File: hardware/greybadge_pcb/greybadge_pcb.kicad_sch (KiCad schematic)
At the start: 73 parts, among them J1 Conn_02x05_Row_Letter_First, J2 Conn_02x05_Row_Letter_First, J3 Conn_02x05_Row_Letter_First, J4 Conn_02x05_Row_Letter_First, SW1 SW_Push, SW2 SW_Push, SW3 SW_Push, SW4 SW_Push, SW5 SW_Push, SW6 SW_Push, SW7 SW_Push, U1 TLV62568DBV, U2 TLV62568DBV, U3 TLV73325PDBV

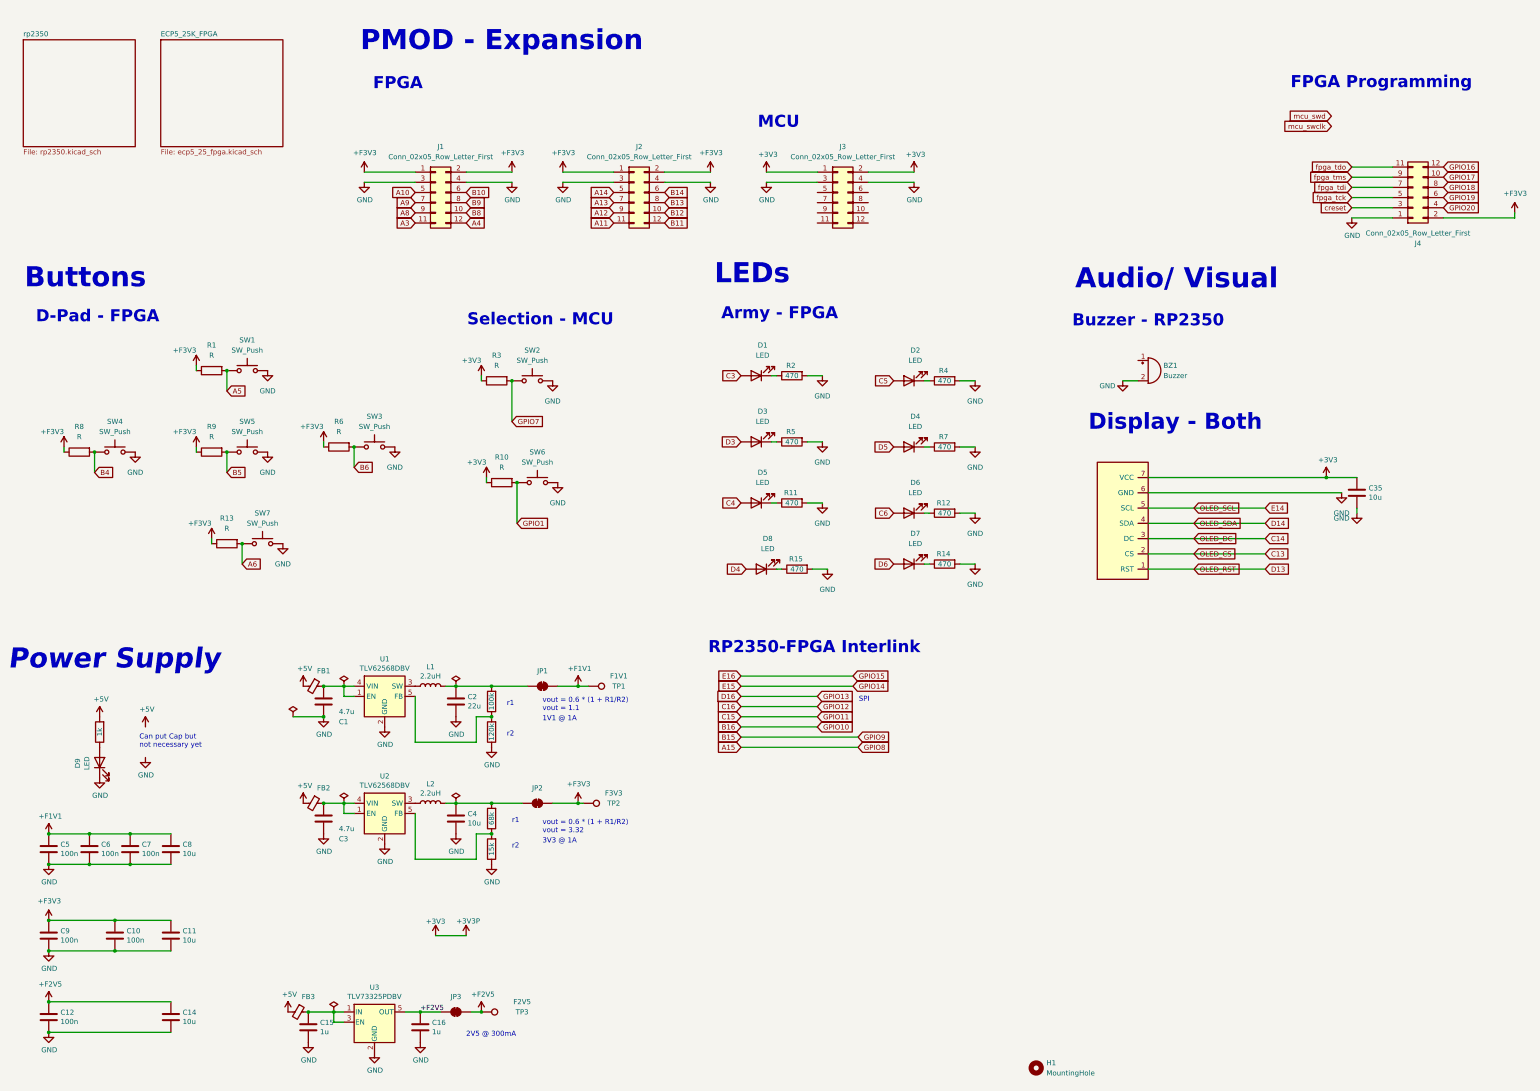
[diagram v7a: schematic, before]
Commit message: feat: add lipo support
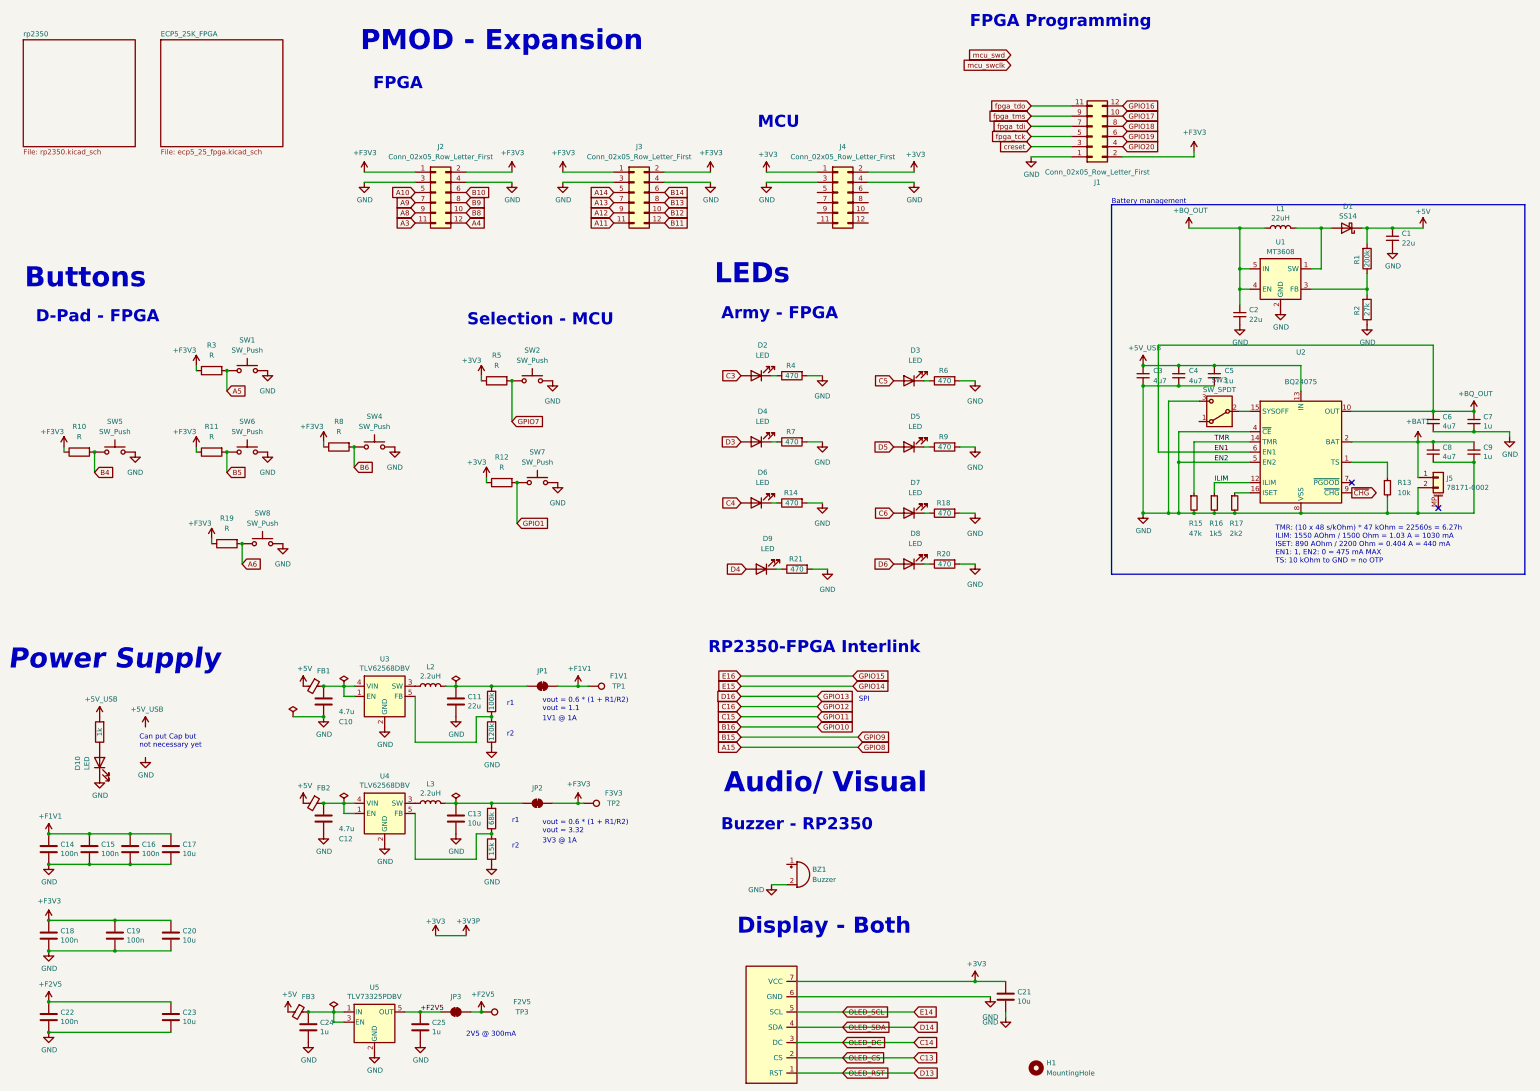
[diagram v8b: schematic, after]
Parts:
- added C1, C2: 22u, Capacitor_SMD:C_0402_1005Metric, symbol Device:C_Small
- added C3, C4, C6, C8: 4u7, Capacitor_SMD:C_0402_1005Metric, symbol Device:C_Small
- added C5, C7, C9: 1u, Capacitor_SMD:C_0402_1005Metric, symbol Device:C_Small
- added D1: SS14, Diode_SMD:D_SMA, symbol Diode:SS14
- added J5: 78171-0002, Connector_JST:JST_PH_S2B-PH-SM4-TB_1x02-1MP_P2.00mm_Horizontal, symbol Connector_Generic_MountingPin:Conn_01x02_MountingPin
- added L1: 22uH, Inductor_SMD:L_Taiyo-Yuden_NR-40xx, symbol Device:L
- added R1: 200k, Resistor_SMD:R_0603_1608Metric_Pad0.98x0.95mm_HandSolder, symbol Device:R
- added R13: 10k, Resistor_SMD:R_0402_1005Metric, symbol Device:R_Small
- added R15: 47k, Resistor_SMD:R_0402_1005Metric, symbol Device:R_Small
- added R16: 1k5, Resistor_SMD:R_0402_1005Metric, symbol Device:R_Small
- added R17: 2k2, Resistor_SMD:R_0402_1005Metric, symbol Device:R_Small
- added R2: 27k, Resistor_SMD:R_0603_1608Metric_Pad0.98x0.95mm_HandSolder, symbol Device:R
- added SW3: SW_SPDT, Button_Switch_SMD:SW_SPDT_CK_JS102011SAQN, symbol Switch:SW_SPDT
- added U1: MT3608, Package_TO_SOT_SMD:SOT-23-6, symbol Regulator_Switching:MT3608
- added U2: BQ24075, Package_DFN_QFN:VQFN-16-1EP_3x3mm_P0.5mm_EP1.6x1.6mm, symbol Battery_Management:BQ24075RGT
- renumbered C1 to C10, C2 to C11, C3 to C12, C4 to C13, C5 to C14, C6 to C15, C7 to C16, C8 to C17, C9 to C18, C10 to C19, C11 to C20, C35 to C21, C12 to C22, C14 to C23, C15 to C24, C16 to C25, D9 to D10, D1 to D2, D2 to D3, D3 to D4, D4 to D5, D5 to D6, D6 to D7, D7 to D8, D8 to D9, J4 to J1, J1 to J2, J2 to J3, J3 to J4, L1 to L2, L2 to L3, R8 to R10, R9 to R11, R10 to R12, R11 to R14, R12 to R18, R13 to R19, R14 to R20, R15 to R21, R16 to R22, R17 to R23, R18 to R24, R19 to R25, R20 to R26, R1 to R3, R2 to R4, R3 to R5, R4 to R6, R5 to R7, R6 to R8, R7 to R9, SW3 to SW4, SW4 to SW5, SW5 to SW6, SW6 to SW7, SW7 to SW8, U1 to U3, U2 to U4, U3 to U5
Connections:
- net +5V: now also C1.1, D1.1 (K), R1.2; no longer R23.2
- net GND: now also C1.2, C2.2, C3.2, C4.2, C5.2, C6.2, C7.2, C8.2, C9.2, J5.2 (Pin_2), R13.2, R15.2, R16.2, R17.2, R2.1, SW3.3 (C), U1.2 (GND), U2.17 (VSS), U2.4 (~{CE}), U2.5 (EN2), U2.8 (VSS)
- new net: D1.2 (A), L1.2, U1.1 (SW)
- new net: R1.1, R2.2, U1.3 (FB)
- new net: SW3.2 (B), U2.15 (SYSOFF)
- new net: R13.1, U2.1 (TS)
- new net: R17.1, U2.16 (ISET)
- new net +5V_USB: C3.1, C4.1, C5.1, R23.2, U2.13 (IN)
- new net +BATT: C8.1, C9.1, J5.1 (Pin_1), U2.2 (BAT), U2.3 (BAT)
- new net +BQ_OUT: C2.1, C6.1, C7.1, L1.1, U1.4 (EN), U1.5 (IN), U2.10 (OUT), U2.11 (OUT), U2.6 (EN1)
- new net ILIM: R16.1, U2.12 (ILIM)
- new net TMR: R15.1, U2.14 (TMR)
- new net ~{CHG}: U2.9 (~{CHG})
- no-connect marks 0 -> 2
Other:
- note added: "Battery management"
- note added: "TMR: (10 x 48 s/kOhm) * 47 kOhm = 22560s = 6.27h ILIM: 1550 AOhm / 1500 Ohm = 1.03 A = 1030 mA ISET: 890 AOhm / 2200 Ohm = 0.404 A = 440 mA EN1: 1, EN2: 0 = 475 mA MAX TS: 10 kOhm to GND = no OTP"
- moved on the sheet: BZ1, C21, J1
